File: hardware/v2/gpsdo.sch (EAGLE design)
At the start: 80 parts, among them IC1 74HCT125N, IC2 74HCT125N, IC3 78L05, IC5 78L09, Q2 2N2222, U1 LMC6482DIL, U2 MAR-4, U3 MAR-4

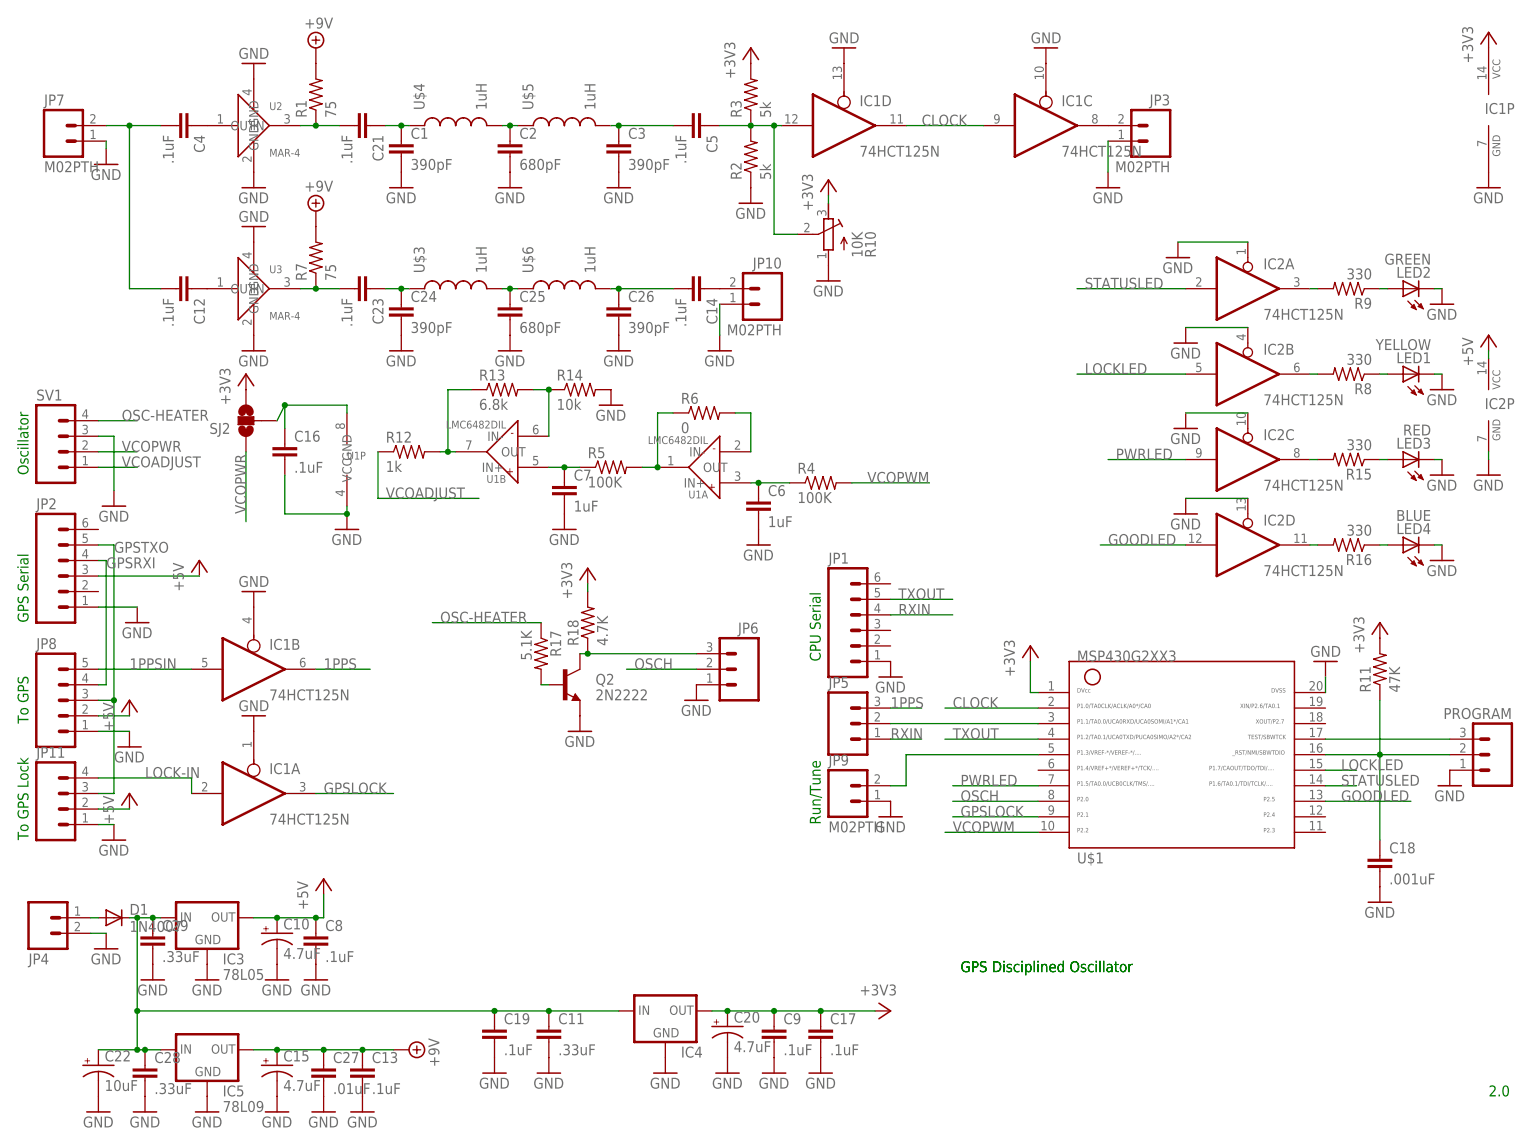
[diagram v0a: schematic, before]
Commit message: Rename components
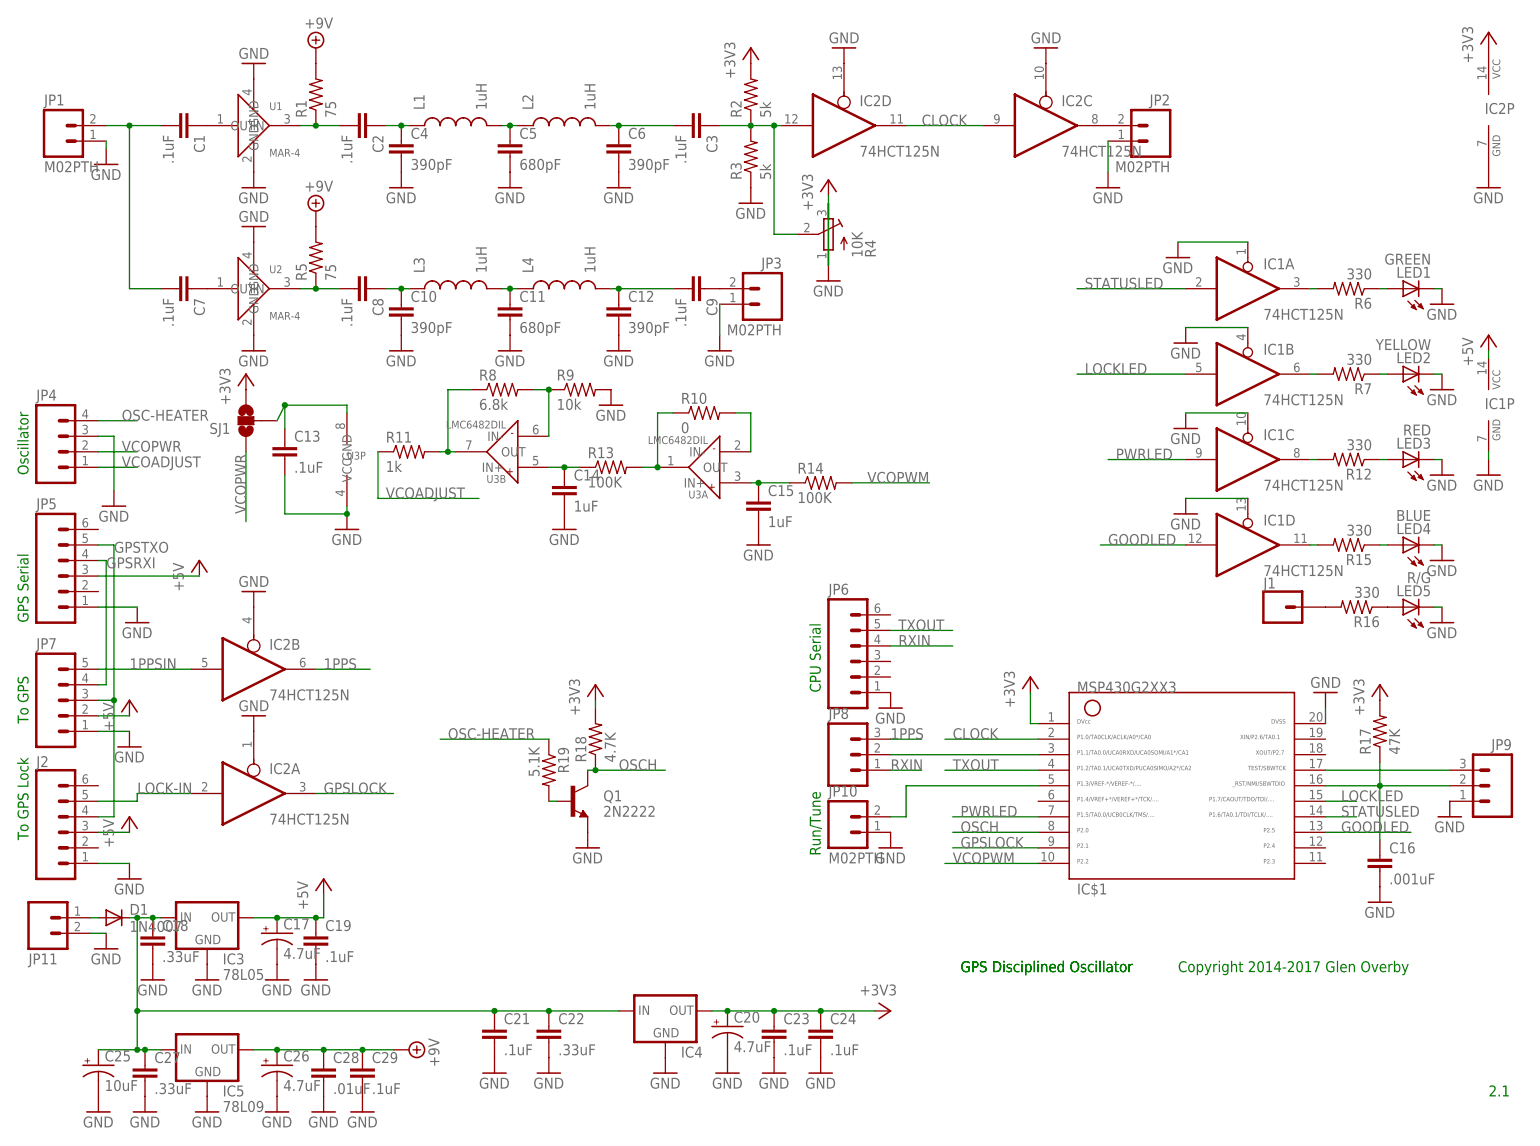
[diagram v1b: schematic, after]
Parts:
- removed PROGRAM: (no value), SparkFun:M03PTH
- removed Q2: 2N2222, SparkFun:TRANSISTOR_NPNTO92
- removed SV1: (no value), SparkFun-Connectors:M04PTH
- removed U$1: G2XX3---N20, TI_MSP430_v16:G2XX3---N20
- added IC$1: G2XX3---N20, TI_MSP430_v16:G2XX3---N20
- added J1: (no value), SparkFun-Connectors:CONN_01
- added J2: (no value), SparkFun-Connectors:CONN_06SILK_FEMALE_PTH
- added LED5: R/G, led:LED3MM
- added Q1: 2N2222, SparkFun:TRANSISTOR_NPNTO92
- added R19: 5.1K, resistor:R-US_0207/2V
- C1, C3: value 390pF -> .1uF; device zener:CAPPTH -> SparkFun:CAPPTH
- C10: value 4.7uF -> 390pF; device SparkFun-Capacitors:10UF-16V-10%(TANT) -> zener:CAPPTH
- C11: value .33uF -> 680pF; device SparkFun-Capacitors:CAPPTH -> zener:CAPPTH
- C12, C4: value .1uF -> 390pF; device SparkFun:CAPPTH -> zener:CAPPTH
- C13: device SparkFun-Capacitors:CAPPTH -> SparkFun-Capacitors:CAPPTH1
- C14: value .1uF -> 1uF; device SparkFun:CAPPTH -> SparkFun-Passives:CAPPTH
- C15: value 4.7uF -> 1uF; device SparkFun-Capacitors:10UF-16V-10%(TANT) -> SparkFun-Passives:CAPPTH
- C16: value .1uF -> .001uF; device SparkFun-Capacitors:CAPPTH1 -> SparkFun-Capacitors:CAPPTH
- C17: value .1uF -> 4.7uF; device SparkFun-Capacitors:CAPPTH -> SparkFun-Capacitors:10UF-16V-10%(TANT)
- C18: value .001uF -> .33uF
- C2: value 680pF -> .1uF; device zener:CAPPTH -> SparkFun:CAPPTH
- C21, C23: device SparkFun:CAPPTH -> SparkFun-Capacitors:CAPPTH
- C22: value 10uF -> .33uF; device SparkFun-Passives:CAP_POLPTH2 -> SparkFun-Capacitors:CAPPTH
- C24: value 390pF -> .1uF; device zener:CAPPTH -> SparkFun-Capacitors:CAPPTH
- C25: value 680pF -> 10uF; device zener:CAPPTH -> SparkFun-Passives:CAP_POLPTH2
- C26: value 390pF -> 4.7uF; device zener:CAPPTH -> SparkFun-Capacitors:10UF-16V-10%(TANT)
- C27: value .01uF -> .33uF
- C28: value .33uF -> .01uF
- C29: value .33uF -> .1uF
- C5: value .1uF -> 680pF; device SparkFun:CAPPTH -> zener:CAPPTH
- C6: value 1uF -> 390pF; device SparkFun-Passives:CAPPTH -> zener:CAPPTH
- C7: value 1uF -> .1uF; device SparkFun-Passives:CAPPTH -> SparkFun:CAPPTH
- C8, C9: device SparkFun-Capacitors:CAPPTH -> SparkFun:CAPPTH
- IC1: device 74xx-us:74LS125N -> 74xx-eu:74HCT125N
- IC2: device 74xx-eu:74HCT125N -> 74xx-us:74LS125N
- JP1, JP2: value (none) -> M02PTH; device SparkFun-Connectors:M06SILK_FEMALE_PTH -> SparkFun-Connectors:M02PTH
- JP11: device SparkFun-Connectors:M04PTH -> SparkFun:M02PTH
- JP4: device SparkFun:M02PTH -> SparkFun-Connectors:M04PTH
- JP5, JP6: device SparkFun:M03PTH -> SparkFun-Connectors:M06SILK_FEMALE_PTH
- JP7: value M02PTH -> (none); device SparkFun-Connectors:M02PTH -> SparkFun:M05PTH
- JP8: device SparkFun:M05PTH -> SparkFun:M03PTH
- JP9: value M02PTH -> (none); device SparkFun-Connectors:M02PTH -> SparkFun:M03PTH
- LED1: value YELLOW -> GREEN
- LED2: value GREEN -> YELLOW
- R10: value 10K -> 0; device resistor:R-TRIMM3296W -> resistor:R-US_0207/2V
- R11: value 47K -> 1k
- R12: value 1k -> 330
- R13: value 6.8k -> 100K
- R14: value 10k -> 100K
- R17: value 5.1K -> 47K
- R4: value 100K -> 10K; device resistor:R-US_0207/2V -> resistor:R-TRIMM3296W
- R5: value 100K -> 75
- R6: value 0 -> 330
- R7: value 75 -> 330
- R8: value 330 -> 6.8k
- R9: value 330 -> 10k
- U1: value LMC6482DIL -> MAR-4; device overby:LMC6482DIL -> LTC3200:MAR-4
- U3: value MAR-4 -> LMC6482DIL; device LTC3200:MAR-4 -> overby:LMC6482DIL
- renumbered SJ2 to SJ1, U$3 to L3, U$4 to L1, U$5 to L2, U$6 to L4
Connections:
- removed net N$8: JP6.3, Q2.C, R18.1
- new net N$28: LED5.A, R16.1
- new net N$29: J1.1, R16.2
- net +3V3: now also C23.1, C24.1, IC$1.1, IC2P.VCC, R17.2, R2.2, R4.A; no longer C17.1, C9.1, IC1P.VCC, R10.A, R11.2, R3.2, U$1.1
- net +5V: now also C17.+, C19.1, IC1P.VCC, J2.3, JP5.3, JP7.2; no longer C10.+, C8.1, IC2P.VCC, JP11.2, JP2.3, JP8.2
- net +9V: now also C26.+, C28.1, C29.1, R5.2; no longer C13.1, C15.+, C27.1, R7.2
- net 1PPS: now also IC2B.O, JP8.3; no longer IC1B.O, JP5.3
- net 1PPSIN: now also IC2B.I, JP7.5; no longer IC1B.I, JP8.5
- net CLOCK: now also IC$1.2, IC2C.I, IC2D.O; no longer IC1C.I, IC1D.O, U$1.2
- net GND: now also C10.2, C12.2, C14.2, C15.2, C17.-, C21.2, C22.2, C23.2, C25.-, C26.-, C4.2, C5.2, IC$1.20, J2.1, JP11.2, JP4.3, JP5.1, LED5.C, Q1.E, R3.1, R4.E, R9.2, U1.GND@2, U1.GND@4, U3P.GND; no longer C1.2, C10.-, C15.-, C17.2, C2.2, C22.-, C25.2, C26.2, C3.2, C7.2, C8.2, C9.2, JP11.1, JP4.2, JP8.1, PROGRAM.1, Q2.E, R10.E, R14.2, R2.1, SV1.3, U$1.20, U1P.GND, U3.GND@2, U3.GND@4
- net GOODLED: now also IC$1.13, IC1D.I; no longer IC2D.I, U$1.13
- net GPSLOCK: now also IC$1.9, IC2A.O; no longer IC1A.O, U$1.9
- net GPSRXI: now also JP5.4, JP7.4; no longer JP2.4, JP8.4
- net GPSTXO: now also J2.4, JP5.5, JP7.3; no longer JP11.3, JP2.5, JP8.3
- net LOCK-IN: now also IC2A.I, J2.5; no longer IC1A.I, JP11.4
- net LOCKLED: now also IC$1.15, IC1B.I; no longer IC2B.I, U$1.15
- net N$1: now also LED2.A, R7.1; no longer LED1.A, R8.1
- net N$10: now also C2.2, U1.OUT; no longer C21.2, U2.OUT
- net N$11: now also C3.1, IC2D.I, R2.1, R3.2, R4.S; no longer C5.1, IC1D.I, R10.S, R2.2, R3.1
- net N$12: now also LED1.A, R6.1; no longer LED2.A, R9.1
- net N$13: now also R11.2, R8.1, U3B.OUT; no longer R12.2, R13.1, U1B.OUT
- net N$14: now also C1.2, C7.2, JP1.2; no longer C12.2, C4.2, JP7.2
- net N$15: now also R10.2, U3A.IN-; no longer R6.2, U1A.IN-
- net N$16: now also C11.1; no longer C25.1
- net N$17: now also JP11.1; no longer JP4.1
- net N$18: now also C12.1, C9.2; no longer C14.2, C26.1
- net N$19: now also IC$1.5, JP10.2; no longer JP9.2, U$1.5
- net N$2: now also C5.1; no longer C2.1
- net N$20: now also IC1C.O, R12.2; no longer IC2C.O, R15.2
- net N$21: now also IC1D.O, R15.2; no longer IC2D.O, R16.2
- net N$22: now also C8.2, R5.1, U2.OUT; no longer C23.2, R7.1, U3.OUT
- net N$23: now also C16.1, IC$1.16, JP9.2, R17.1; no longer C18.1, PROGRAM.2, R11.1, U$1.16
- net N$24: now also C10.1, C8.1; no longer C23.1, C24.1
- net N$25: now also C7.1, U2.IN; no longer C12.1, U3.IN
- net N$26: now also C9.1, JP3.2; no longer C14.1, JP10.2
- net N$27: now also IC$1.17, JP9.3; no longer PROGRAM.3, U$1.17
- net N$3: now also C3.2, C6.1; no longer C3.1, C5.2
- net N$30: now also IC2C.O, JP2.2; no longer IC1C.O, JP3.2
- net N$31: now also C13.1, U3P.VCC; no longer C16.1, U1P.VCC
- net N$33: now also C2.1, C4.1; no longer C1.1, C21.1
- net N$35: now also IC1A.O, R6.2; no longer IC2A.O, R9.2
- net N$36: now also IC1B.O, R7.2; no longer IC2B.O, R8.2
- net N$37: now also R8.2, R9.1, U3B.IN-; no longer R13.2, R14.1, U1B.IN-
- net N$39: now also R12.1; no longer R15.1
- net N$4: now also C1.1, U1.IN; no longer C4.1, U2.IN
- net N$40: now also R15.1; no longer R16.1
- net N$41: now also Q1.B, R19.2; no longer Q2.B, R17.2
- net N$5: now also C14.1, R13.1, U3B.IN+; no longer C7.1, R5.1, U1B.IN+
- net N$6: now also R10.1, R13.2, U3A.OUT; no longer R5.2, R6.1, U1A.OUT
- net N$7: now also C15.1, R14.1, U3A.IN+; no longer C6.1, R4.1, U1A.IN+
- net N$9: now also IC$1.3, JP8.2; no longer JP5.2, U$1.3
- net OSC-HEATER: now also JP4.4, R19.1; no longer R17.1, SV1.4
- net OSCH: now also IC$1.8, Q1.C, R18.1; no longer JP6.2, U$1.8
- net PWRIN: now also C18.1, C21.1, C22.1, C25.+, C27.1; no longer C11.1, C19.1, C22.+, C28.1, C29.1
- net PWRLED: now also IC$1.7, IC1C.I; no longer IC2C.I, U$1.7
- net RXIN: now also JP6.4, JP8.1; no longer JP1.4, JP5.1
- net STATUSLED: now also IC$1.14, IC1A.I; no longer IC2A.I, U$1.14
- net TXOUT: now also IC$1.4, JP6.5; no longer JP1.5, U$1.4
- net VCOADJUST: now also JP4.1, R11.1; no longer R12.1, SV1.1
- net VCOPWM: now also IC$1.10, R14.2; no longer R4.2, U$1.10
- net VCOPWR: now also JP4.2; no longer SV1.2
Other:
- note added: "2.1"
- note added: "Copyright 2014-2017 Glen Overby"
- note removed: "2.0"
- moved on the sheet: C1, C11, C12, C13, C14, C16, C18, C19, C2, C21, C23, C24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
